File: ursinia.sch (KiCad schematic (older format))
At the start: 13 parts, among them J1 NEIGHBOR1, J2 NEIGHBOR2, J7 BONUS_ROW, U1 M24C02-FMN6TP

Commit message: complete design
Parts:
- added J10, J11, J12, J14, J15, J16, J5, J6, J8: GROVE-CONNECTOR-DIP_4P-2.0_, OPL_Connectors:HW4-2.0, symbol OPL_Connectors:GROVE-CONNECTOR-DIP_4P-2.0_
- added J13, J17, J3, J4, J9: GROVE-CONNECTOR-DIP_4P-2.0_, OPL_Connectors:HW4-2.0-90D, symbol OPL_Connectors:GROVE-CONNECTOR-DIP_4P-2.0_
- added R2, R3: 2k, Resistor_SMD:R_0603_1608Metric_Pad1.05x0.95mm_HandSolder, symbol Device:R
- C1, JP1, JP2, JP3, R1, U1: Note (none) -> DNP
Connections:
- net ADC0_0: now also J3.1
- net ADC0_5: now also J3.2
- net GND: now also J10.4, J11.4, J12.4, J13.4, J14.4, J15.4, J16.4, J17.4, J3.4, J4.4, J5.4, J6.4, J8.4, J9.4
- net I2C0_SCL: now also J10.1, J11.1, J12.1, J13.1
- net I2C0_SDA: now also J10.2, J11.2, J12.2, J13.2
- net P1_16: now also J9.2
- net P2_10: now also J16.2
- net P2_11: now also J16.1
- net P2_3: now also J17.2, R3.2
- net P2_4: now also J17.1, R2.2
- net P4_3: now also J4.2
- net P4_4: now also J5.1
- net P4_5: now also J5.2
- net P5_4: now also J8.1
- net P5_5: now also J8.2
- net P5_6: now also J15.2
- net P5_7: now also J15.1
- net P6_4: now also J14.2
- net P6_5: now also J14.1
- net P7_0: now also J6.1
- net P7_1: now also J6.2
- net P7_7: now also J4.1
- net P9_6: now also J9.1
- net VCC: now also J10.3, J11.3, J12.3, J13.3, J14.3, J15.3, J16.3, J17.3, J3.3, J4.3, J5.3, J6.3, J8.3, J9.3, R2.1, R3.1
- no-connect marks 10 -> 70
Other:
- note added: "Analog"
- note added: "Analog/Digital"
- note added: "Digital"
- note added: "Digital/MCPWM"
- note added: "Digital/SGPIO/MCPWM"
- note added: "Digital/SGPIO/SCT"
- note added: "I2C"
- note added: "UART/Digital"
- note added: "USART0"
- note added: "USART1"
- note added: "USART2"
- note added: "USART3/I2C1"
- note added: "option:\nIf you wish to use J17 for\nI2C, populate R2 and R3."
- note removed: "How to Design a Neighbor:\nhttps://github.com/greatscottgadgets/greatfet/wiki/How-to-Design-a-Neighbor"
- note removed: "J7 is optional"
- note removed: "Pins with no-connect flags may affect Azalea (mainboard)\nboot. Do not use them unless you study Azalea to\nunderstand the consequences."

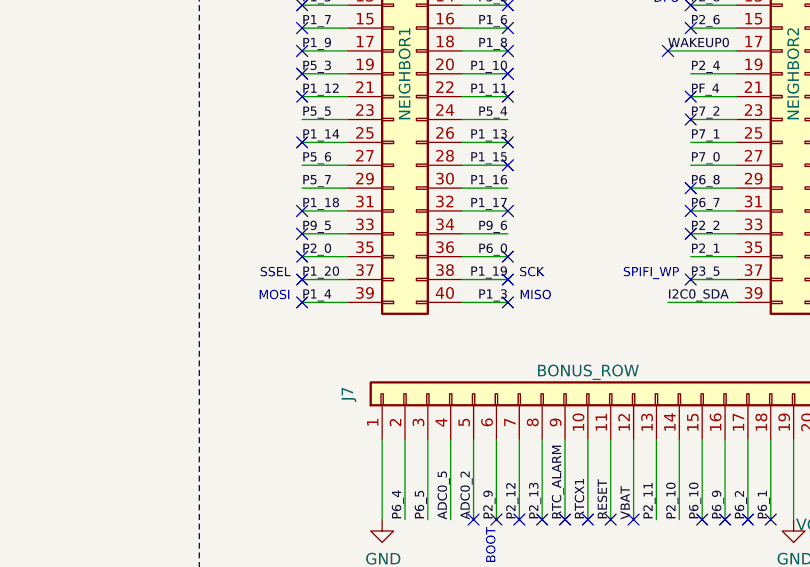
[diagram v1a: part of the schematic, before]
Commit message: adopt OSHWA convention for SPI signal names https://www.oshwa.org/a-resolution-to-redefine-spi-signal-names
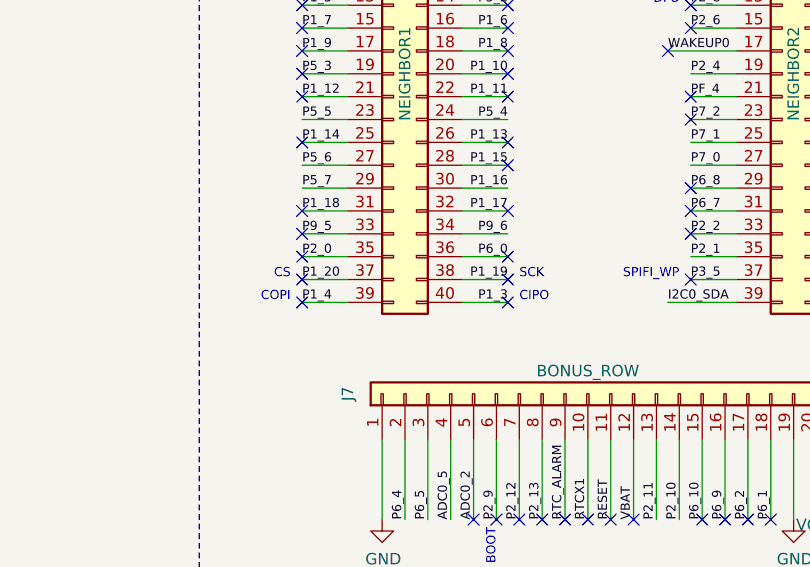
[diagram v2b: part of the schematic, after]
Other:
- note added: "CIPO"
- note added: "COPI"
- note added: "CS"
- note removed: "MISO"
- note removed: "MOSI"
- note removed: "SSEL"
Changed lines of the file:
@@
 P2_0
 Text Notes 14300 2850 0    40   ~ 0
-MISO
+CIPO
 Text Notes 13300 2850 2    40   ~ 0
-MOSI
+COPI
 Text Notes 14300 2750 0    40   ~ 0
 SCK
 Text Notes 13300 2750 2    40   ~ 0
-SSEL
+CS
 Text Label 16050 2850 2    40   ~ 0
 I2C0_SCL
